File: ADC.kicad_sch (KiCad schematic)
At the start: 16 parts, among them J4 CURRENT INPUTS, J6 DIFFERENTIAL INPUT, J8 ANALOG VOLTAGE INPUTS, U12 REF3333, U13 ADS1261

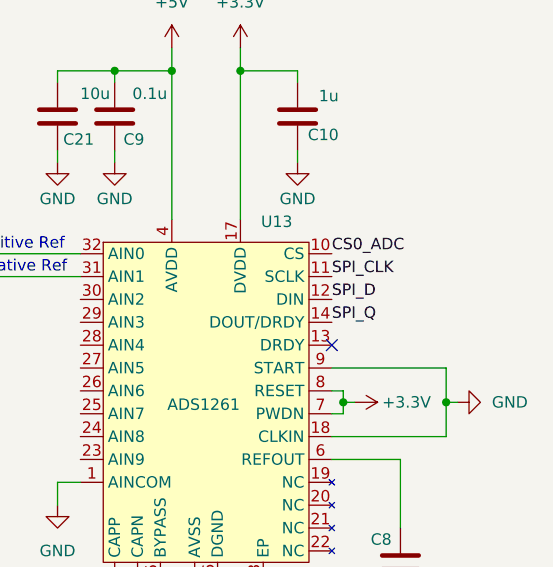
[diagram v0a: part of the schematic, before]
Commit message: changed net labels to global labels
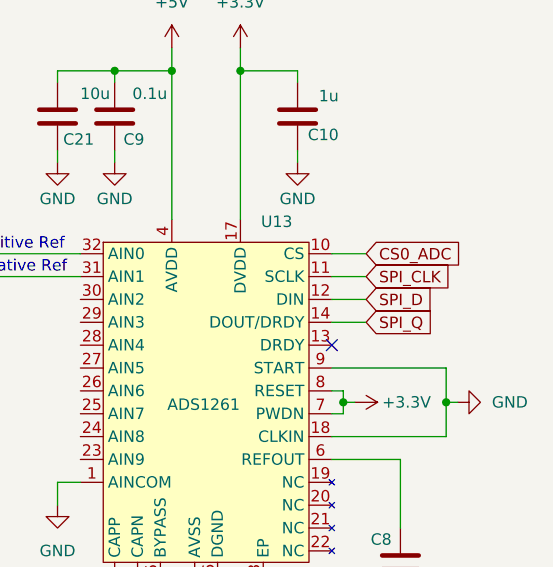
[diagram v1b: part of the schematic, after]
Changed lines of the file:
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@@
+	(wire
+		(pts
+			(xy 181.61 85.09) (xy 185.42 85.09)
+		)
+		(stroke
+			(width 0)
+			(type default)
+		)
+	)
 	(wire
 		(pts
@@
 	(wire
 		(pts
+			(xy 181.61 82.55) (xy 185.42 82.55)
+		)
+		(stroke
+			(width 0)
+			(type default)
+		)
+	)
+	(wire
+		(pts
 			(xy 132.08 74.93) (xy 135.89 74.93)
 		)
@@
 	(wire
 		(pts
+			(xy 181.61 90.17) (xy 185.42 90.17)
+		)
+		(stroke
+			(width 0)
+			(type default)
+		)
+	)
+	(wire
+		(pts
 			(xy 109.22 31.75) (xy 111.76 31.75)
 		)
@@
 	(wire
 		(pts
+			(xy 181.61 87.63) (xy 185.42 87.63)
+		)
+		(stroke
+			(width 0)
+			(type default)
+		)
+	)
+	(wire
+		(pts
 			(xy 162.56 124.46) (xy 162.56 132.08)
 		)
@@
 		)
 	)
-	(label "SPI_D"
-		(at 181.61 87.63 0)
+	(global_label "CS0_ADC"
+		(shape input)
+		(at 185.42 82.55 0)
+		(fields_autoplaced yes)
 		(effects
 			(font
 				(size 1.27 1.27)
 			)
-			(justify left bottom)
-		)
-	)
-	(label "SPI_CLK"
-		(at 181.61 85.09 0)
+			(justify left)
+		)
+		(property "Intersheetrefs" "${INTERSHEET_REFS}"
+			(at 196.6904 82.55 0)
+			(hide yes)
+			(show_name no)
+			(do_not_autoplace no)
+			(effects
+				(font
+					(size 1.27 1.27)
+				)
+				(justify left)
+			)
+		)
+	)
+	(global_label "SPI_Q"
+		(shape input)
+		(at 185.42 90.17 0)
+		(fields_autoplaced yes)
 		(effects
 			(font
 				(size 1.27 1.27)
 			)
-			(justify left bottom)
-		)
-	)
-	(label "CS0_ADC"
-		(at 181.61 82.55 0)
+			(justify left)
+		)
+		(property "Intersheetrefs" "${INTERSHEET_REFS}"
+			(at 193.7876 90.17 0)
+			(hide yes)
+			(show_name no)
+			(do_not_autoplace no)
+			(effects
+				(font
+					(size 1.27 1.27)
+				)
+				(justify left)
+			)
+		)
+	)
+	(global_label "SPI_CLK"
+		(shape input)
+		(at 185.42 85.09 0)
+		(fields_autoplaced yes)
 		(effects
 			(font
 				(size 1.27 1.27)
 			)
-			(justify left bottom)
-		)
-	)
-	(label "SPI_Q"
-		(at 181.61 90.17 0)
+			(justify left)
+		)
+		(property "Intersheetrefs" "${INTERSHEET_REFS}"
+			(at 196.0252 85.09 0)
+			(hide yes)
+			(show_name no)
+			(do_not_autoplace no)
+			(effects
+				(font
+					(size 1.27 1.27)
+				)
+				(justify left)
+			)
+		)
+	)
+	(global_label "SPI_D"
+		(shape input)
+		(at 185.42 87.63 0)
+		(fields_autoplaced yes)
 		(effects
 			(font
 				(size 1.27 1.27)
 			)
-			(justify left bottom)
-		)
-	)
+			(justify left)
+		)
+		(property "Intersheetrefs" "${INTERSHEET_REFS}"
+			(at 193.7271 87.63 0)
+			(hide yes)
+			(show_name no)
+			(do_not_autoplace no)
+			(effects
+				(font
+					(size 1.27 1.27)
+				)
+				(justify left)
+			)
+		)
+	)

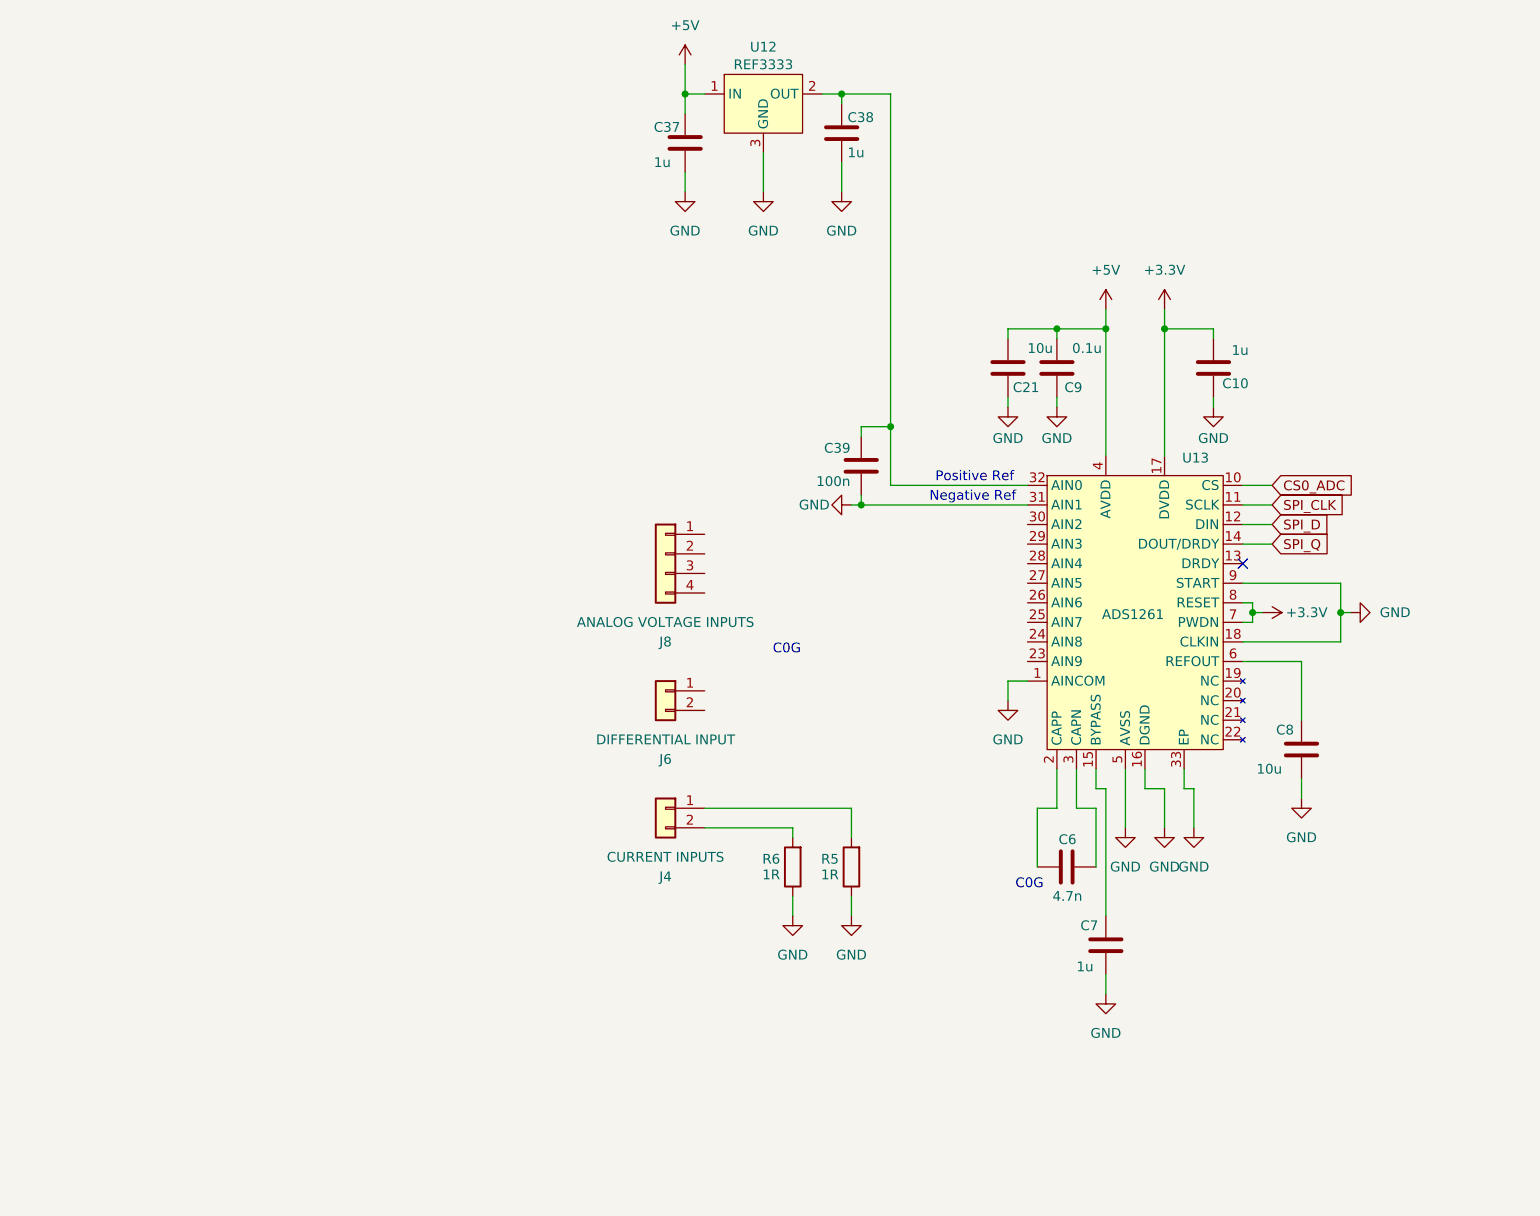
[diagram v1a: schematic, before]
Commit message: added gnd to inputs
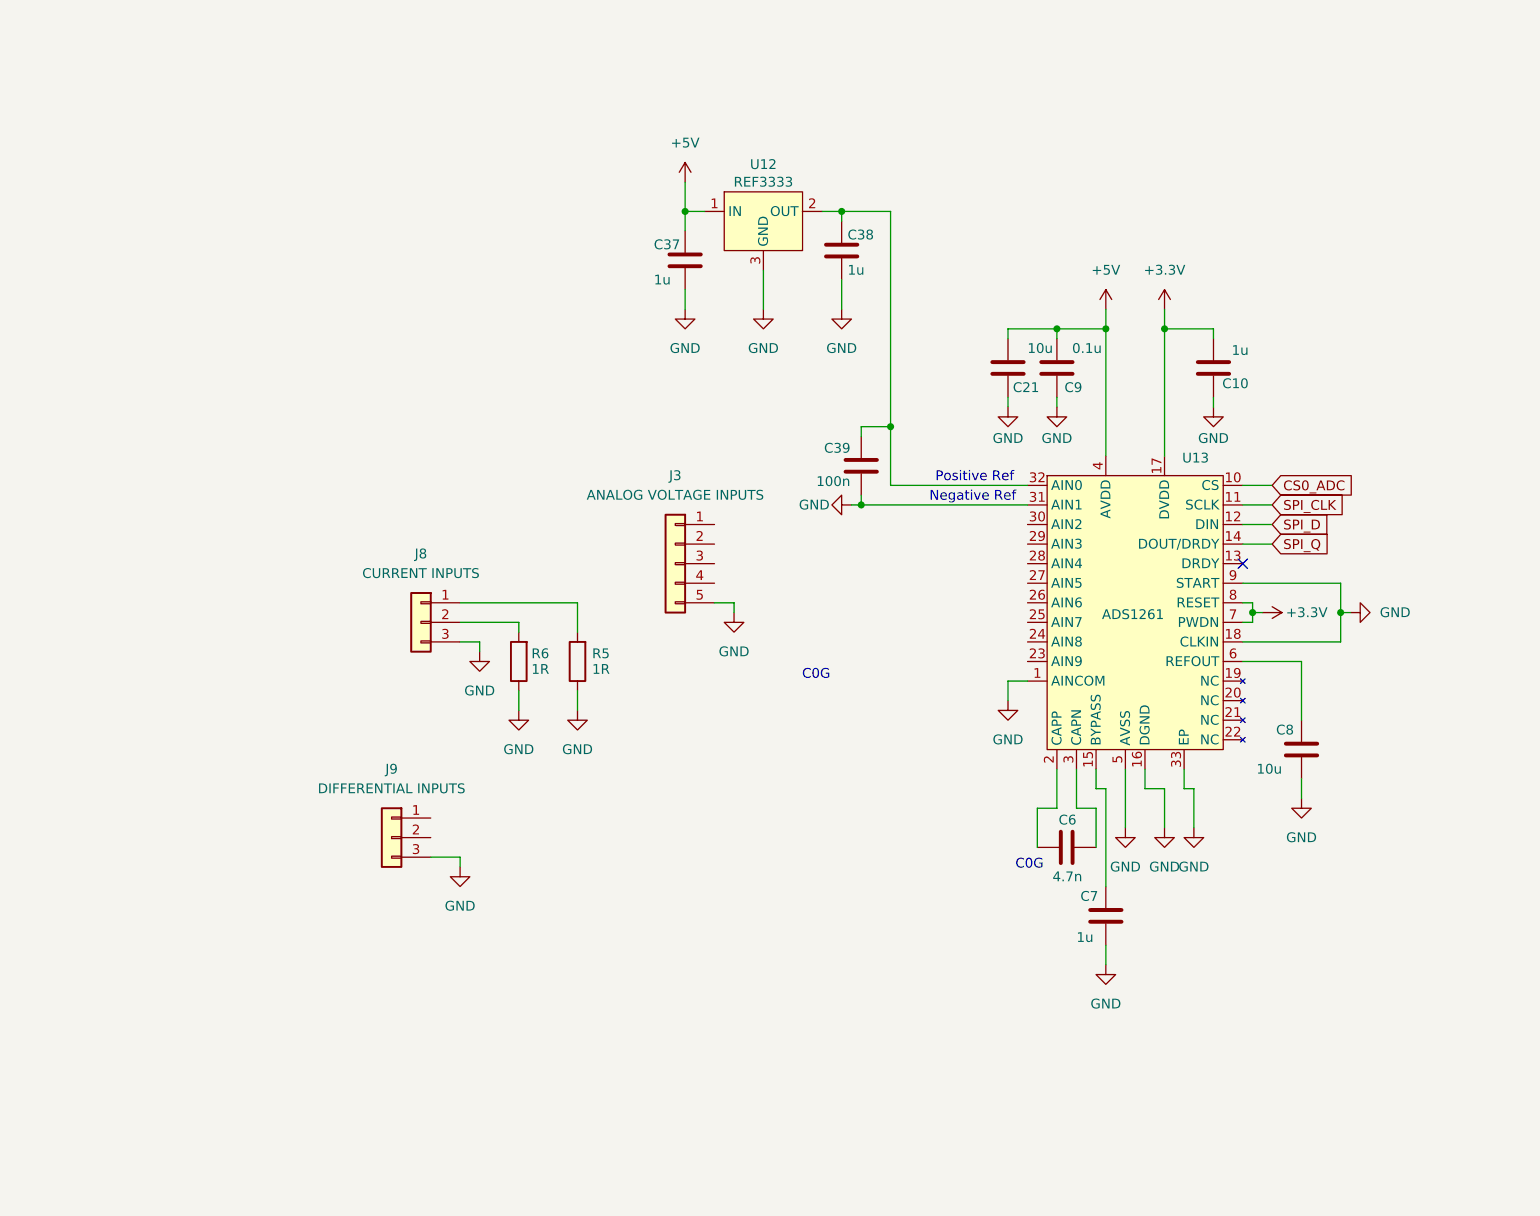
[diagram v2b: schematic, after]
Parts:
- removed J4: CURRENT INPUTS, symbol Connector_Generic:Conn_01x02
- removed J6: DIFFERENTIAL INPUT, symbol Connector_Generic:Conn_01x02
- removed J8: ANALOG VOLTAGE INPUTS, symbol Connector_Generic:Conn_01x04
- added J3: ANALOG VOLTAGE INPUTS, symbol Connector_Generic:Conn_01x05
- added J8: CURRENT INPUTS, symbol Connector_Generic:Conn_01x03
- added J9: DIFFERENTIAL INPUTS, symbol Connector_Generic:Conn_01x03
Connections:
- net GND: now also J3.5 (Pin_5), J8.3 (Pin_3), J9.3 (Pin_3)
- net at R6.2: now also J8.2 (Pin_2)
- net at R5.2: now also J8.1 (Pin_1)
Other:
- moved on the sheet: C37, C38, C6, C7, R5, R6, U12

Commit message: 9/18/2026 schematic work
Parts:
- added C11, C12, C13, C14: 1u, symbol Device:C
- added C22: 0.01u, symbol Device:C
- added C23, C24: 1n, symbol Device:C
- added R10, R11, R12, R13, R14, R7, R8, R9: 100R, symbol Device:R
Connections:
- net GND: now also C11.2, C12.2, C13.2, C14.2, C23.2, C24.1
- net at J8.2 (Pin_2), R6.2: now also R14.1
- net at J8.1 (Pin_1), R5.2: now also R13.1
- net at J9.1 (Pin_1): now also R11.1
- net at J9.2 (Pin_2): now also R12.1
- net at J3.1 (Pin_1): now also R7.1
- net at J3.2 (Pin_2): now also R8.1
- net at J3.3 (Pin_3): now also R9.1
- net at J3.4 (Pin_4): now also R10.1
- net at U13.23 (AIN9): now also R14.2
- net at U13.24 (AIN8): now also R13.2
- net at U13.25 (AIN7): now also C22.2, C24.2, R12.2
- net at U13.26 (AIN6): now also C22.1, C23.1, R11.2
- net at U13.27 (AIN5): now also C14.1, R10.2
- net at U13.28 (AIN4): now also C13.1, R9.2
- net at U13.29 (AIN3): now also C12.1, R8.2
- net at U13.30 (AIN2): now also C11.1, R7.2
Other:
- note added: "All AFE capacitors are C0G"
- note added: "Differential fc = 80 kHz Common mode fc = 1.6 MHz"
- note added: "Noise RC fc = 1.6 kHz"
- moved on the sheet: C10, C21, C37, C38, C39, C6, C7, C8, C9, J3, J8, J9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

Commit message: removed grounds from inputs
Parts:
- removed J3: ANALOG VOLTAGE INPUTS, symbol Connector_Generic:Conn_01x05
- removed J8: CURRENT INPUTS, symbol Connector_Generic:Conn_01x03
- removed J9: DIFFERENTIAL INPUTS, symbol Connector_Generic:Conn_01x03
- added J4: ANALOG VOLTAGE INPUTS, symbol Connector_Generic:Conn_01x04
- added J5: DIFFERENTIAL INPUTS, symbol Connector_Generic:Conn_01x02
- added J6: CURRENT INPUTS, symbol Connector_Generic:Conn_01x02
- renumbered C23 to C10, C24 to C11, C11 to C12, C12 to C13, C13 to C14, C14 to C15, C22 to C16, C37 to C17, C38 to C18, C39 to C19, C21 to C20, C9 to C21, C6 to C22, C7 to C23, C10 to C24, C8 to C25, R9 to R10, R10 to R11, R5 to R12, R6 to R13, R13 to R14, R14 to R15, R11 to R6, R12 to R7, R7 to R8, R8 to R9, U12 to U4, U13 to U5
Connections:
- net at R13.2, R15.1: now also J6.2 (Pin_2)
- net at R9.1: now also J4.2 (Pin_2)
- net at R8.1: now also J4.1 (Pin_1)
- net at R12.2, R14.1: now also J6.1 (Pin_1)
- net at R7.1: now also J5.2 (Pin_2)
- net at R11.1: now also J4.4 (Pin_4)
- net at R6.1: now also J5.1 (Pin_1)
- net at R10.1: now also J4.3 (Pin_3)

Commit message: 9/20/2026 schematic work
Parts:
- C10, C11: footprint (none) -> Capacitor_SMD:C_1206_3216Metric_Pad1.33x1.80mm_HandSolder; MPN (none) -> GRM31C5C3A102JWA3L; Mouser Link (none) -> https://www.mouser.com/en/ProductDetail/Murata-Electronics/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
- C12, C13, C14, C15: value 1u -> 1n; footprint (none) -> Capacitor_SMD:C_1206_3216Metric_Pad1.33x1.80mm_HandSolder; MPN (none) -> GRM31C5C3A102JWA3L; Mouser Link (none) -> https://www.mouser.com/en/ProductDetail/Murata-Electronics/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
- C16: footprint (none) -> Capacitor_SMD:C_1206_3216Metric_Pad1.33x1.80mm_HandSolder; MPN (none) -> GRM31C5C2J103JWA3L; Mouser Link (none) -> https://www.mouser.com/en/ProductDetail/Murata-Electronics/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
- C17, C18, C23, C24: footprint (none) -> Capacitor_SMD:C_1206_3216Metric_Pad1.33x1.80mm_HandSolder; MPN (none) -> GRM31CR71E105KA01L; Mouser Link (none) -> https://www.mouser.com/en/ProductDetail/Murata-Electronics/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
- C19: value 100n -> 0.1u; footprint (none) -> Capacitor_SMD:C_1206_3216Metric_Pad1.33x1.80mm_HandSolder; MPN (none) -> GRM31CR72E104KW03L; Mouser Link (none) -> https://www.mouser.com/en/ProductDetail/Murata-Electronics/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
- C20, C25: footprint (none) -> Capacitor_SMD:C_1206_3216Metric_Pad1.33x1.80mm_HandSolder; MPN (none) -> GCM31CC71E106KA03K; Mouser Link (none) -> https://www.mouser.com/en/ProductDetail/Murata-Electronics/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
- C21: footprint (none) -> Capacitor_SMD:C_1206_3216Metric_Pad1.33x1.80mm_HandSolder; MPN (none) -> GRM31CR72E104KW03L; Mouser Link (none) -> https://www.mouser.com/en/ProductDetail/Murata-Electronics/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
- C22: footprint (none) -> Capacitor_SMD:C_1206_3216Metric_Pad1.33x1.80mm_HandSolder; MPN (none) -> GCM3195C2A472FA16D; Mouser Link (none) -> https://www.mouser.com/en/ProductDetail/Murata-Electronics/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
- J5: value DIFFERENTIAL INPUTS -> DIFFERENTIAL INPUT
- R10: renamed from R8; footprint (none) -> Resistor_SMD:R_1206_3216Metric_Pad1.30x1.75mm_HandSolder; MPN (none) -> RC1206DR-07100RL; Mouser Link (none) -> https://www.mouser.com/en/ProductDetail/YAGEO/RC1206DR-0710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
- R11: renamed from R9; footprint (none) -> Resistor_SMD:R_1206_3216Metric_Pad1.30x1.75mm_HandSolder; MPN (none) -> RC1206DR-07100RL; Mouser Link (none) -> https://www.mouser.com/en/ProductDetail/YAGEO/RC1206DR-0710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
- R12: renamed from R10; footprint (none) -> Resistor_SMD:R_1206_3216Metric_Pad1.30x1.75mm_HandSolder; MPN (none) -> RC1206DR-07100RL; Mouser Link (none) -> https://www.mouser.com/en/ProductDetail/YAGEO/RC1206DR-0710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
- R13: renamed from R11; footprint (none) -> Resistor_SMD:R_1206_3216Metric_Pad1.30x1.75mm_HandSolder; MPN (none) -> RC1206DR-07100RL; Mouser Link (none) -> https://www.mouser.com/en/ProductDetail/YAGEO/RC1206DR-0710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
- R14: renamed from R12; footprint (none) -> Resistor_SMD:R_1206_3216Metric_Pad1.30x1.75mm_HandSolder; MPN (none) -> AC1206FR-071RL; Mouser Link (none) -> https://www.mouser.com/en/ProductDetail/YAGEO/AC1206FR-071R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
- R15: renamed from R13; footprint (none) -> Resistor_SMD:R_1206_3216Metric_Pad1.30x1.75mm_HandSolder; MPN (none) -> AC1206FR-071RL; Mouser Link (none) -> https://www.mouser.com/en/ProductDetail/YAGEO/AC1206FR-071R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
- R16: renamed from R14; footprint (none) -> Resistor_SMD:R_1206_3216Metric_Pad1.30x1.75mm_HandSolder; MPN (none) -> RC1206DR-07100RL; Mouser Link (none) -> https://www.mouser.com/en/ProductDetail/YAGEO/RC1206DR-0710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
- R17: renamed from R15; footprint (none) -> Resistor_SMD:R_1206_3216Metric_Pad1.30x1.75mm_HandSolder; MPN (none) -> RC1206DR-07100RL; Mouser Link (none) -> https://www.mouser.com/en/ProductDetail/YAGEO/RC1206DR-0710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
- R8: renamed from R6; footprint (none) -> Resistor_SMD:R_1206_3216Metric_Pad1.30x1.75mm_HandSolder; MPN (none) -> RC1206DR-07100RL; Mouser Link (none) -> https://www.mouser.com/en/ProductDetail/YAGEO/RC1206DR-0710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
- R9: renamed from R7; footprint (none) -> Resistor_SMD:R_1206_3216Metric_Pad1.30x1.75mm_HandSolder; MPN (none) -> RC1206DR-07100RL; Mouser Link (none) -> https://www.mouser.com/en/ProductDetail/YAGEO/RC1206DR-0710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
- U5: renamed from U4; Mouser Link (none) -> https://www.mouser.com/en/ProductDetail/Texas-Instruments/R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
- U6: renamed from U5; footprint Package_DFN_QFN:QFN-32-1EP_5x5mm_P0.5mm_EP3.45x3.45mm -> Package_DFN_QFN:QFN-32-1EP_5x5mm_P0.5mm_EP3.45x3.45mm_ThermalVias; Mouser Link (none) -> https://www.mouser.com/en/ProductDetail/Texas-Instruments/A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
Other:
- note added: "Analog 1"
- note added: "Analog 2"
- note added: "Analog 3"
- note added: "Analog 4"
- note added: "Current 1"
- note added: "Current 2"
- note added: "Diff. Analog +"
- note added: "Diff. Analog -"
- note added: "Noise RC fc = 1.6 MHz"
- note removed: "Noise RC fc = 1.6 kHz"
- company: Slap DAQ -> Faster Than Sound
- title: ADC -> SlapDAQ - MCU
- moved on the sheet: C18
